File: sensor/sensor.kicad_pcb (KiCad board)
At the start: 2 copper layers, 19.6 x 13.2 mm, 4 parts, among them J2 Conn_01x03, U1 KMZ60

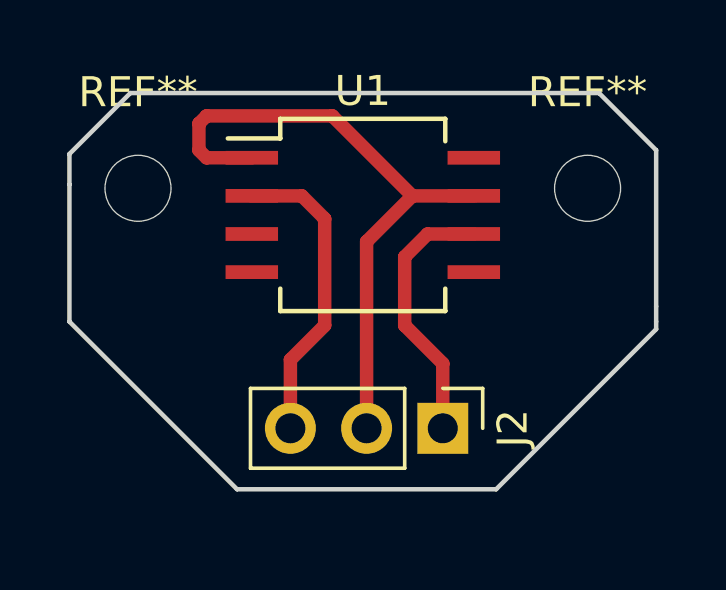
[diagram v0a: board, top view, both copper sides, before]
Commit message: sensor board double output update
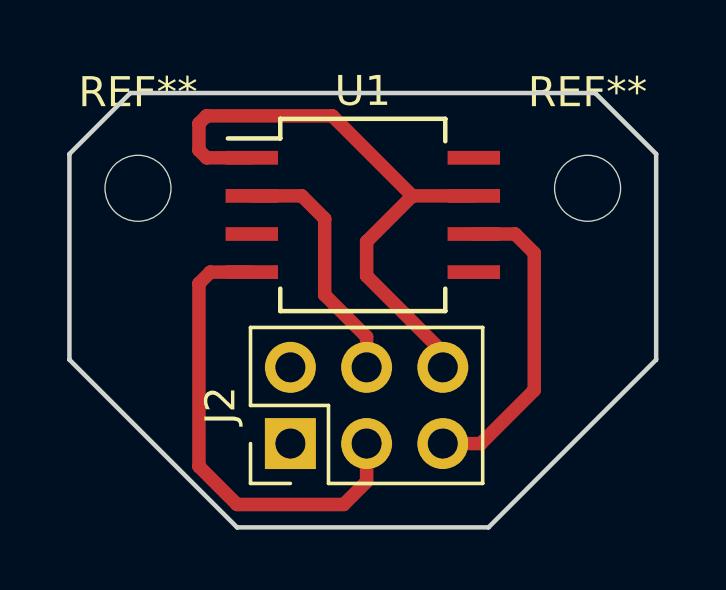
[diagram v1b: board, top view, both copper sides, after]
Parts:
- J2: value Conn_01x03 -> Conn_02x03_Counter_Clockwise; footprint Pin_Headers:Pin_Header_Straight_1x03_Pitch2.54mm -> Pin_Headers:Pin_Header_Straight_2x03_Pitch2.54mm
- moved J2 5.11 mm to (148.1, 116.8), turned to 90 degrees
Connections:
- J2 pad 2: Net-(J1-Pad6) -> Net-(J1-Pad2)
- J2 pad 3: Net-(J1-Pad2) -> Net-(J1-Pad6)
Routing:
- net Net-(J1-Pad4): track 0.00 -> 15.7 mm
- net Net-(J1-Pad2): track 10.2 -> 8.28 mm
- net Net-(J1-Pad6): track 8.86 -> 10.6 mm
- net Net-(J1-Pad1): track 21.5 -> 20.5 mm
- removed copper zone on F.Cu, net Net-(J1-Pad6)
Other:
- board size 19.6 x 13.2 mm -> 19.6 x 14.5 mm
